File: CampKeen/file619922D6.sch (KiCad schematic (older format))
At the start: 40 parts, among them Q20 2N7000, Q21 2N7000, Q22 2N7000, Q23 2N7000, Q24 2N7000, Q25 2N7000, Q26 2N7000, Q27 2N7000, Q28 2N7000, Q29 2N7000

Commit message: some annotation.
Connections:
- net +5V renamed +5VL
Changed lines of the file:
@@
 Wire Wire Line
 	2450 1600 2450 1550
-$Comp
-L power:+5V #PWR?
-U 1 1 61994D03
-P 2450 950
-AR Path="/62665296/61994D03" Ref="#PWR?"  Part="1"
-AR Path="/6479D118/61994D03" Ref="#PWR?"  Part="1"
-AR Path="/627AE565/61994D03" Ref="#PWR?"  Part="1"
-AR Path="/619922D7/61994D03" Ref="#PWR0105"  Part="1"
-F 0 "#PWR0105" H 2450 800 50  0001 C CNN
-F 1 "+5V" H 2465 1123 50  0000 C CNN
-F 2 "" H 2450 950 50  0001 C CNN
-F 3 "" H 2450 950 50  0001 C CNN
-	1    2450 950
-	1    0    0    -1
-$EndComp
 Wire Wire Line
 	2450 1100 2450 950
@@
 Wire Wire Line
 	2450 3300 2450 3250
-$Comp
-L power:+5V #PWR?
-U 1 1 619C5CF6
-P 2450 2650
-AR Path="/62665296/619C5CF6" Ref="#PWR?"  Part="1"
-AR Path="/6479D118/619C5CF6" Ref="#PWR?"  Part="1"
-AR Path="/627AE565/619C5CF6" Ref="#PWR?"  Part="1"
-AR Path="/619922D7/619C5CF6" Ref="#PWR0107"  Part="1"
-F 0 "#PWR0107" H 2450 2500 50  0001 C CNN
-F 1 "+5V" H 2465 2823 50  0000 C CNN
-F 2 "" H 2450 2650 50  0001 C CNN
-F 3 "" H 2450 2650 50  0001 C CNN
-	1    2450 2650
-	1    0    0    -1
-$EndComp
 Wire Wire Line
 	2450 2800 2450 2650
@@
 Wire Wire Line
 	2450 4900 2450 4850
-$Comp
-L power:+5V #PWR?
-U 1 1 619F4CB4
-P 2450 4250
-AR Path="/62665296/619F4CB4" Ref="#PWR?"  Part="1"
-AR Path="/6479D118/619F4CB4" Ref="#PWR?"  Part="1"
-AR Path="/627AE565/619F4CB4" Ref="#PWR?"  Part="1"
-AR Path="/619922D7/619F4CB4" Ref="#PWR0109"  Part="1"
-F 0 "#PWR0109" H 2450 4100 50  0001 C CNN
-F 1 "+5V" H 2465 4423 50  0000 C CNN
-F 2 "" H 2450 4250 50  0001 C CNN
-F 3 "" H 2450 4250 50  0001 C CNN
-	1    2450 4250
-	1    0    0    -1
-$EndComp
 Wire Wire Line
 	2450 4400 2450 4250
@@
 Wire Wire Line
 	2450 6600 2450 6550
-$Comp
-L power:+5V #PWR?
-U 1 1 619FB7BE
-P 2450 5950
-AR Path="/62665296/619FB7BE" Ref="#PWR?"  Part="1"
-AR Path="/6479D118/619FB7BE" Ref="#PWR?"  Part="1"
-AR Path="/627AE565/619FB7BE" Ref="#PWR?"  Part="1"
-AR Path="/619922D7/619FB7BE" Ref="#PWR0111"  Part="1"
-F 0 "#PWR0111" H 2450 5800 50  0001 C CNN
-F 1 "+5V" H 2465 6123 50  0000 C CNN
-F 2 "" H 2450 5950 50  0001 C CNN
-F 3 "" H 2450 5950 50  0001 C CNN
-	1    2450 5950
-	1    0    0    -1
-$EndComp
 Wire Wire Line
 	2450 6100 2450 5950
@@
 Wire Wire Line
 	5750 1600 5750 1550
-$Comp
-L power:+5V #PWR?
-U 1 1 61AA89BA
-P 5750 950
-AR Path="/62665296/61AA89BA" Ref="#PWR?"  Part="1"
-AR Path="/6479D118/61AA89BA" Ref="#PWR?"  Part="1"
-AR Path="/627AE565/61AA89BA" Ref="#PWR?"  Part="1"
-AR Path="/619922D7/61AA89BA" Ref="#PWR0113"  Part="1"
-F 0 "#PWR0113" H 5750 800 50  0001 C CNN
-F 1 "+5V" H 5765 1123 50  0000 C CNN
-F 2 "" H 5750 950 50  0001 C CNN
-F 3 "" H 5750 950 50  0001 C CNN
-	1    5750 950
-	1    0    0    -1
-$EndComp
 Wire Wire Line
 	5750 1100 5750 950
@@
 Wire Wire Line
 	8150 1600 8150 1550
-$Comp
-L power:+5V #PWR?
-U 1 1 61AC655C
-P 8150 950
-AR Path="/62665296/61AC655C" Ref="#PWR?"  Part="1"
-AR Path="/6479D118/61AC655C" Ref="#PWR?"  Part="1"
-AR Path="/627AE565/61AC655C" Ref="#PWR?"  Part="1"
-AR Path="/619922D7/61AC655C" Ref="#PWR0121"  Part="1"
-F 0 "#PWR0121" H 8150 800 50  0001 C CNN
-F 1 "+5V" H 8165 1123 50  0000 C CNN
-F 2 "" H 8150 950 50  0001 C CNN
-F 3 "" H 8150 950 50  0001 C CNN
-	1    8150 950
-	1    0    0    -1
-$EndComp
 Wire Wire Line
 	8150 1100 8150 950
@@
 Wire Wire Line
 	5750 3350 5750 3300
-$Comp
-L power:+5V #PWR?
-U 1 1 61ACB046
-P 5750 2700
-AR Path="/62665296/61ACB046" Ref="#PWR?"  Part="1"
-AR Path="/6479D118/61ACB046" Ref="#PWR?"  Part="1"
-AR Path="/627AE565/61ACB046" Ref="#PWR?"  Part="1"
-AR Path="/619922D7/61ACB046" Ref="#PWR0115"  Part="1"
-F 0 "#PWR0115" H 5750 2550 50  0001 C CNN
-F 1 "+5V" H 5765 2873 50  0000 C CNN
-F 2 "" H 5750 2700 50  0001 C CNN
-F 3 "" H 5750 2700 50  0001 C CNN
-	1    5750 2700
-	1    0    0    -1
-$EndComp
 Wire Wire Line
 	5750 2850 5750 2700
@@
 Wire Wire Line
 	8150 3350 8150 3300
-$Comp
-L power:+5V #PWR?
-U 1 1 61ACFF01
-P 8150 2700
-AR Path="/62665296/61ACFF01" Ref="#PWR?"  Part="1"
-AR Path="/6479D118/61ACFF01" Ref="#PWR?"  Part="1"
-AR Path="/627AE565/61ACFF01" Ref="#PWR?"  Part="1"
-AR Path="/619922D7/61ACFF01" Ref="#PWR0123"  Part="1"
-F 0 "#PWR0123" H 8150 2550 50  0001 C CNN
-F 1 "+5V" H 8165 2873 50  0000 C CNN
-F 2 "" H 8150 2700 50  0001 C CNN
-F 3 "" H 8150 2700 50  0001 C CNN
-	1    8150 2700
-	1    0    0    -1
-$EndComp
 Wire Wire Line
 	8150 2850 8150 2700
@@
 Wire Wire Line
 	5750 5100 5750 5050
-$Comp
-L power:+5V #PWR?
-U 1 1 61AD6017
-P 5750 4450
-AR Path="/62665296/61AD6017" Ref="#PWR?"  Part="1"
-AR Path="/6479D118/61AD6017" Ref="#PWR?"  Part="1"
-AR Path="/627AE565/61AD6017" Ref="#PWR?"  Part="1"
-AR Path="/619922D7/61AD6017" Ref="#PWR0117"  Part="1"
-F 0 "#PWR0117" H 5750 4300 50  0001 C CNN
-F 1 "+5V" H 5765 4623 50  0000 C CNN
-F 2 "" H 5750 4450 50  0001 C CNN
-F 3 "" H 5750 4450 50  0001 C CNN
-	1    5750 4450
-	1    0    0    -1
-$EndComp
 Wire Wire Line
 	5750 4600 5750 4450
@@
 Wire Wire Line
 	8100 5100 8100 5050
-$Comp
-L power:+5V #PWR?
-U 1 1 61ADB4DA
-P 8100 4450
-AR Path="/62665296/61ADB4DA" Ref="#PWR?"  Part="1"
-AR Path="/6479D118/61ADB4DA" Ref="#PWR?"  Part="1"
-AR Path="/627AE565/61ADB4DA" Ref="#PWR?"  Part="1"
-AR Path="/619922D7/61ADB4DA" Ref="#PWR0119"  Part="1"
-F 0 "#PWR0119" H 8100 4300 50  0001 C CNN
-F 1 "+5V" H 8115 4623 50  0000 C CNN
-F 2 "" H 8100 4450 50  0001 C CNN
-F 3 "" H 8100 4450 50  0001 C CNN
-	1    8100 4450
-	1    0    0    -1
-$EndComp
 Wire Wire Line
 	8100 4600 8100 4450
@@
 Wire Wire Line
 	7150 5100 7150 4800
+$Comp
+L power:+5VL #PWR0107
+U 1 1 61BBDD38
+P 2450 950
+F 0 "#PWR0107" H 2450 800 50  0001 C CNN
+F 1 "+5VL" H 2465 1123 50  0000 C CNN
+F 2 "" H 2450 950 50  0001 C CNN
+F 3 "" H 2450 950 50  0001 C CNN
+	1    2450 950
+	1    0    0    -1
+$EndComp
+$Comp
+L power:+5VL #PWR0115
+U 1 1 61BC5B51
+P 5750 950
+F 0 "#PWR0115" H 5750 800 50  0001 C CNN
+F 1 "+5VL" H 5765 1123 50  0000 C CNN
+F 2 "" H 5750 950 50  0001 C CNN
+F 3 "" H 5750 950 50  0001 C CNN
+	1    5750 950
+	1    0    0    -1
+$EndComp
+$Comp
+L power:+5VL #PWR0123
+U 1 1 61BCD965
+P 8150 950
+F 0 "#PWR0123" H 8150 800 50  0001 C CNN
+F 1 "+5VL" H 8165 1123 50  0000 C CNN
+F 2 "" H 8150 950 50  0001 C CNN
+F 3 "" H 8150 950 50  0001 C CNN
+	1    8150 950
+	1    0    0    -1
+$EndComp
+$Comp
+L power:+5VL #PWR0153
+U 1 1 61BD57E2
+P 8150 2700
+F 0 "#PWR0153" H 8150 2550 50  0001 C CNN
+F 1 "+5VL" H 8165 2873 50  0000 C CNN
+F 2 "" H 8150 2700 50  0001 C CNN
+F 3 "" H 8150 2700 50  0001 C CNN
+	1    8150 2700
+	1    0    0    -1
+$EndComp
+$Comp
+L power:+5VL #PWR0117
+U 1 1 61BDD617
+P 5750 2700
+F 0 "#PWR0117" H 5750 2550 50  0001 C CNN
+F 1 "+5VL" H 5765 2873 50  0000 C CNN
+F 2 "" H 5750 2700 50  0001 C CNN
+F 3 "" H 5750 2700 50  0001 C CNN
+	1    5750 2700
+	1    0    0    -1
+$EndComp
+$Comp
+L power:+5VL #PWR0109
+U 1 1 61BE57AF
+P 2450 2650
+F 0 "#PWR0109" H 2450 2500 50  0001 C CNN
+F 1 "+5VL" H 2465 2823 50  0000 C CNN
+F 2 "" H 2450 2650 50  0001 C CNN
+F 3 "" H 2450 2650 50  0001 C CNN
+	1    2450 2650
+	1    0    0    -1
+$EndComp
+$Comp
+L power:+5VL #PWR0111
+U 1 1 61BED6DC
+P 2450 4250
+F 0 "#PWR0111" H 2450 4100 50  0001 C CNN
+F 1 "+5VL" H 2465 4423 50  0000 C CNN
+F 2 "" H 2450 4250 50  0001 C CNN
+F 3 "" H 2450 4250 50  0001 C CNN
+	1    2450 4250
+	1    0    0    -1
+$EndComp
+$Comp
+L power:+5VL #PWR0121
+U 1 1 61BF9767
+P 8100 4450
+F 0 "#PWR0121" H 8100 4300 50  0001 C CNN
+F 1 "+5VL" H 8115 4623 50  0000 C CNN
+F 2 "" H 8100 4450 50  0001 C CNN
+F 3 "" H 8100 4450 50  0001 C CNN
+	1    8100 4450
+	1    0    0    -1
+$EndComp
+$Comp
+L power:+5VL #PWR0119
+U 1 1 61C01846
+P 5750 4450
+F 0 "#PWR0119" H 5750 4300 50  0001 C CNN
+F 1 "+5VL" H 5765 4623 50  0000 C CNN
+F 2 "" H 5750 4450 50  0001 C CNN
+F 3 "" H 5750 4450 50  0001 C CNN
+	1    5750 4450
+	1    0    0    -1
+$EndComp
+$Comp
+L power:+5VL #PWR0113
+U 1 1 61C09647
+P 2450 5950
+F 0 "#PWR0113" H 2450 5800 50  0001 C CNN
+F 1 "+5VL" H 2465 6123 50  0000 C CNN
+F 2 "" H 2450 5950 50  0001 C CNN
+F 3 "" H 2450 5950 50  0001 C CNN
+	1    2450 5950
+	1    0    0    -1
+$EndComp
 $EndSCHEMATC

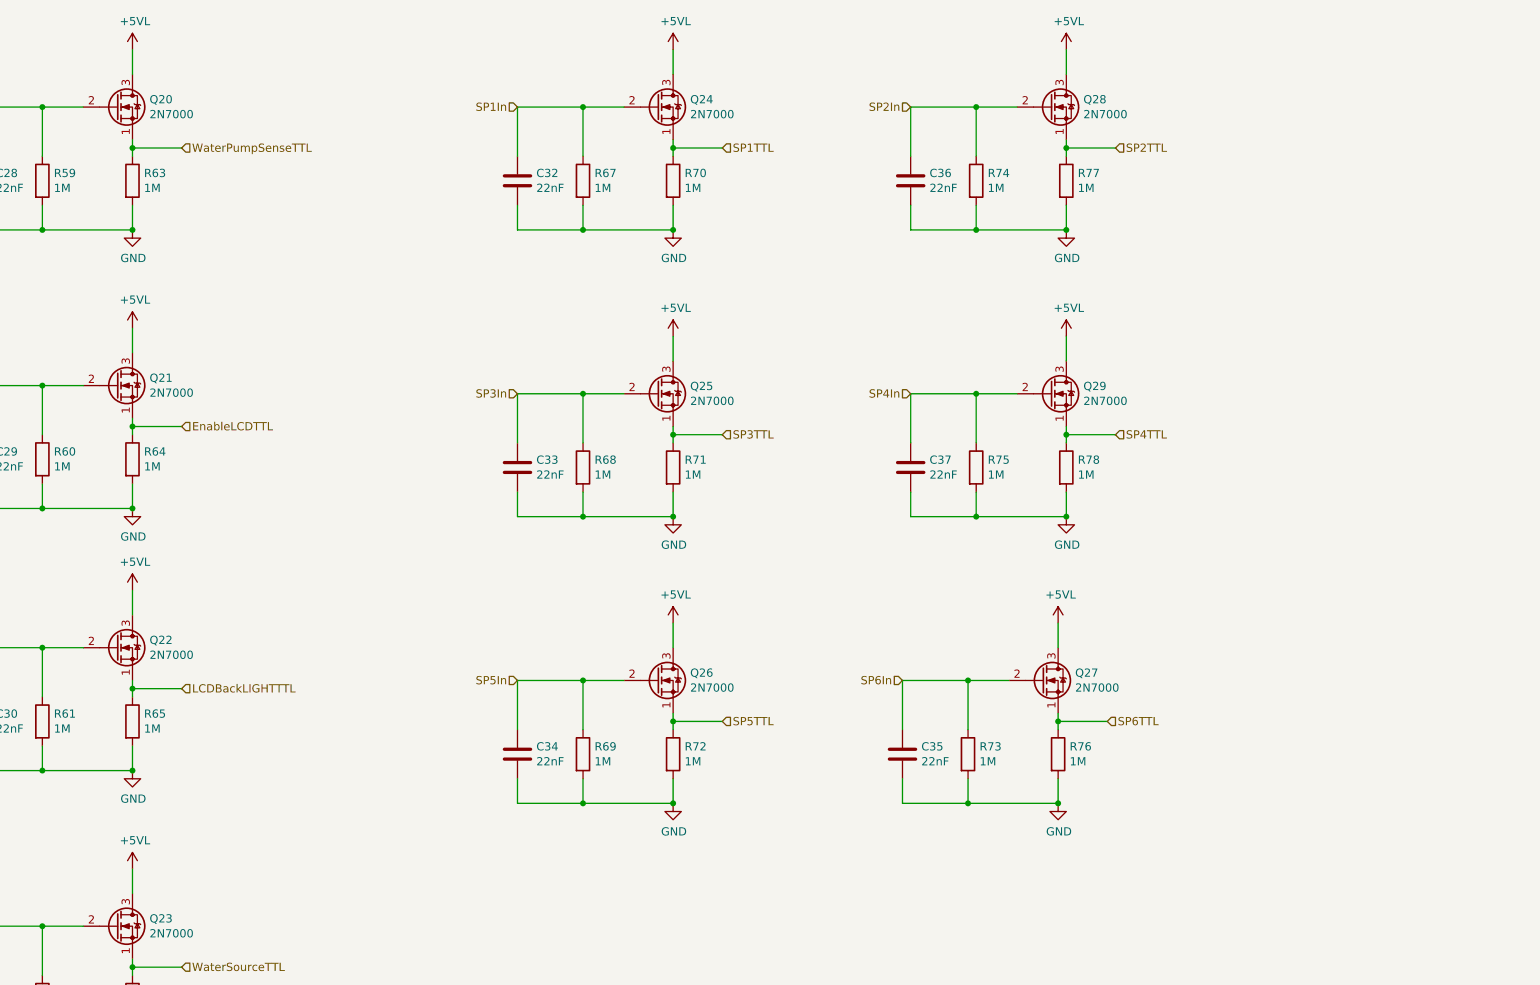
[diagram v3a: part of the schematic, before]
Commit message: wip for working on the input circuits on the board. they are getting upgraded with opto-isolation as i've found that you can burn out the processor board if there is a voltage applied to an input when the system is on and then turned off. for the code fixing some of the LCD display code.
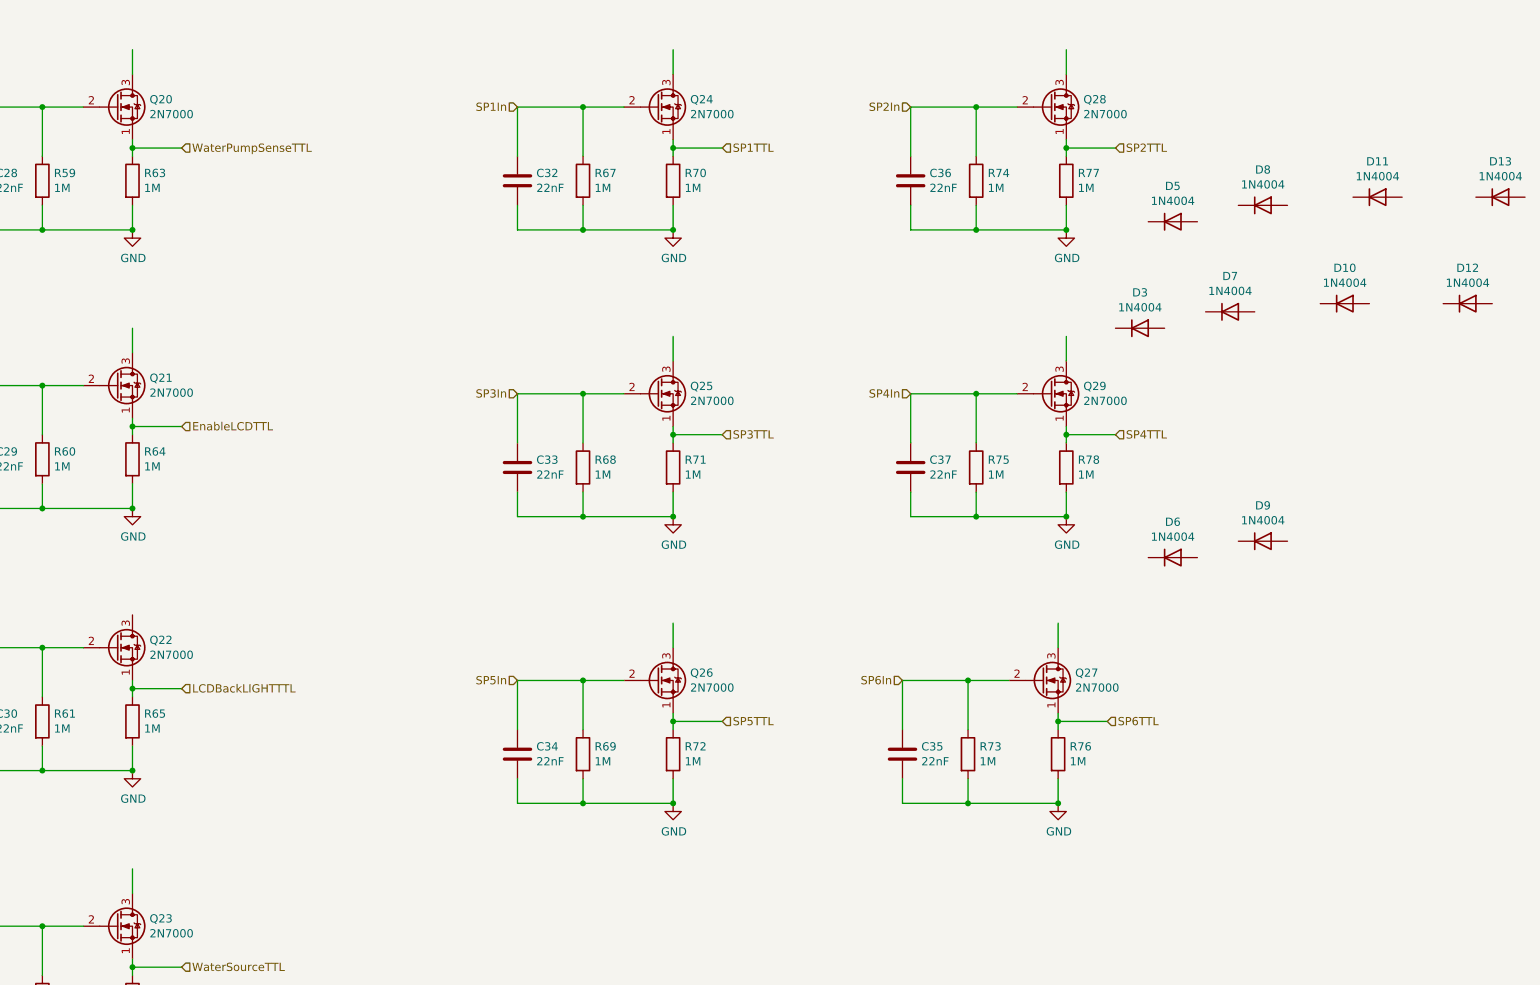
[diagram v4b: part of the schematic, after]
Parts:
- added D10, D11, D12, D13, D3, D5, D6, D7, D8, D9: 1N4004, Diode_THT:D_DO-41_SOD81_P10.16mm_Horizontal, symbol Diode:1N4004
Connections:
- net labels removed: +5VL
- wire segments 130 -> 129
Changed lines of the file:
@@
 	2450 4900 2450 4850
-Wire Wire Line
-	2450 4400 2450 4250
 Wire Wire Line
 	2450 4850 2750 4850
@@
 	7150 5100 7150 4800
 $Comp
-L power:+5VL #PWR0107
-U 1 1 61BBDD38
-P 2450 950
-F 0 "#PWR0107" H 2450 800 50  0001 C CNN
-F 1 "+5VL" H 2465 1123 50  0000 C CNN
-F 2 "" H 2450 950 50  0001 C CNN
-F 3 "" H 2450 950 50  0001 C CNN
-	1    2450 950
-	1    0    0    -1
-$EndComp
-$Comp
-L power:+5VL #PWR0115
-U 1 1 61BC5B51
-P 5750 950
-F 0 "#PWR0115" H 5750 800 50  0001 C CNN
-F 1 "+5VL" H 5765 1123 50  0000 C CNN
-F 2 "" H 5750 950 50  0001 C CNN
-F 3 "" H 5750 950 50  0001 C CNN
-	1    5750 950
-	1    0    0    -1
-$EndComp
-$Comp
-L power:+5VL #PWR0123
-U 1 1 61BCD965
-P 8150 950
-F 0 "#PWR0123" H 8150 800 50  0001 C CNN
-F 1 "+5VL" H 8165 1123 50  0000 C CNN
-F 2 "" H 8150 950 50  0001 C CNN
-F 3 "" H 8150 950 50  0001 C CNN
-	1    8150 950
-	1    0    0    -1
-$EndComp
-$Comp
-L power:+5VL #PWR0153
-U 1 1 61BD57E2
-P 8150 2700
-F 0 "#PWR0153" H 8150 2550 50  0001 C CNN
-F 1 "+5VL" H 8165 2873 50  0000 C CNN
-F 2 "" H 8150 2700 50  0001 C CNN
-F 3 "" H 8150 2700 50  0001 C CNN
-	1    8150 2700
-	1    0    0    -1
-$EndComp
-$Comp
-L power:+5VL #PWR0117
-U 1 1 61BDD617
-P 5750 2700
-F 0 "#PWR0117" H 5750 2550 50  0001 C CNN
-F 1 "+5VL" H 5765 2873 50  0000 C CNN
-F 2 "" H 5750 2700 50  0001 C CNN
-F 3 "" H 5750 2700 50  0001 C CNN
-	1    5750 2700
-	1    0    0    -1
-$EndComp
-$Comp
-L power:+5VL #PWR0109
-U 1 1 61BE57AF
-P 2450 2650
-F 0 "#PWR0109" H 2450 2500 50  0001 C CNN
-F 1 "+5VL" H 2465 2823 50  0000 C CNN
-F 2 "" H 2450 2650 50  0001 C CNN
-F 3 "" H 2450 2650 50  0001 C CNN
-	1    2450 2650
-	1    0    0    -1
-$EndComp
-$Comp
-L power:+5VL #PWR0111
-U 1 1 61BED6DC
-P 2450 4250
-F 0 "#PWR0111" H 2450 4100 50  0001 C CNN
-F 1 "+5VL" H 2465 4423 50  0000 C CNN
-F 2 "" H 2450 4250 50  0001 C CNN
-F 3 "" H 2450 4250 50  0001 C CNN
-	1    2450 4250
-	1    0    0    -1
-$EndComp
-$Comp
-L power:+5VL #PWR0121
-U 1 1 61BF9767
-P 8100 4450
-F 0 "#PWR0121" H 8100 4300 50  0001 C CNN
-F 1 "+5VL" H 8115 4623 50  0000 C CNN
-F 2 "" H 8100 4450 50  0001 C CNN
-F 3 "" H 8100 4450 50  0001 C CNN
-	1    8100 4450
-	1    0    0    -1
-$EndComp
-$Comp
-L power:+5VL #PWR0119
-U 1 1 61C01846
-P 5750 4450
-F 0 "#PWR0119" H 5750 4300 50  0001 C CNN
-F 1 "+5VL" H 5765 4623 50  0000 C CNN
-F 2 "" H 5750 4450 50  0001 C CNN
-F 3 "" H 5750 4450 50  0001 C CNN
-	1    5750 4450
-	1    0    0    -1
-$EndComp
-$Comp
-L power:+5VL #PWR0113
-U 1 1 61C09647
-P 2450 5950
-F 0 "#PWR0113" H 2450 5800 50  0001 C CNN
-F 1 "+5VL" H 2465 6123 50  0000 C CNN
-F 2 "" H 2450 5950 50  0001 C CNN
-F 3 "" H 2450 5950 50  0001 C CNN
-	1    2450 5950
-	1    0    0    -1
-$EndComp
+L Diode:1N4004 D?
+U 1 1 61CCCAE6
+P 8600 2650
+AR Path="/6479D118/61CCCAE6" Ref="D?"  Part="1"
+AR Path="/619922D7/61CCCAE6" Ref="D3"  Part="1"
+F 0 "D3" H 8600 2867 50  0000 C CNN
+F 1 "1N4004" H 8600 2776 50  0000 C CNN
+F 2 "Diode_THT:D_DO-41_SOD81_P10.16mm_Horizontal" H 8600 2475 50  0001 C CNN
+F 3 "http://www.vishay.com/docs/88503/1n4001.pdf" H 8600 2650 50  0001 C CNN
+	1    8600 2650
+	1    0    0    -1
+$EndComp
+$Comp
+L Diode:1N4004 D?
+U 1 1 61CCCAEC
+P 9150 2550
+AR Path="/6479D118/61CCCAEC" Ref="D?"  Part="1"
+AR Path="/619922D7/61CCCAEC" Ref="D7"  Part="1"
+F 0 "D7" H 9150 2767 50  0000 C CNN
+F 1 "1N4004" H 9150 2676 50  0000 C CNN
+F 2 "Diode_THT:D_DO-41_SOD81_P10.16mm_Horizontal" H 9150 2375 50  0001 C CNN
+F 3 "http://www.vishay.com/docs/88503/1n4001.pdf" H 9150 2550 50  0001 C CNN
+	1    9150 2550
+	1    0    0    -1
+$EndComp
+$Comp
+L Diode:1N4004 D?
+U 1 1 61CCCAF2
+P 9850 2500
+AR Path="/6479D118/61CCCAF2" Ref="D?"  Part="1"
+AR Path="/619922D7/61CCCAF2" Ref="D10"  Part="1"
+F 0 "D10" H 9850 2717 50  0000 C CNN
+F 1 "1N4004" H 9850 2626 50  0000 C CNN
+F 2 "Diode_THT:D_DO-41_SOD81_P10.16mm_Horizontal" H 9850 2325 50  0001 C CNN
+F 3 "http://www.vishay.com/docs/88503/1n4001.pdf" H 9850 2500 50  0001 C CNN
+	1    9850 2500
+	1    0    0    -1
+$EndComp
+$Comp
+L Diode:1N4004 D?
+U 1 1 61CCCAF8
+P 10600 2500
+AR Path="/6479D118/61CCCAF8" Ref="D?"  Part="1"
+AR Path="/619922D7/61CCCAF8" Ref="D12"  Part="1"
+F 0 "D12" H 10600 2717 50  0000 C CNN
+F 1 "1N4004" H 10600 2626 50  0000 C CNN
+F 2 "Diode_THT:D_DO-41_SOD81_P10.16mm_Horizontal" H 10600 2325 50  0001 C CNN
+F 3 "http://www.vishay.com/docs/88503/1n4001.pdf" H 10600 2500 50  0001 C CNN
+	1    10600 2500
+	1    0    0    -1
+$EndComp
+$Comp
+L Diode:1N4004 D?
+U 1 1 61CD23F7
+P 8800 2000
+AR Path="/6479D118/61CD23F7" Ref="D?"  Part="1"
+AR Path="/619922D7/61CD23F7" Ref="D5"  Part="1"
+F 0 "D5" H 8800 2217 50  0000 C CNN
+F 1 "1N4004" H 8800 2126 50  0000 C CNN
+F 2 "Diode_THT:D_DO-41_SOD81_P10.16mm_Horizontal" H 8800 1825 50  0001 C CNN
+F 3 "http://www.vishay.com/docs/88503/1n4001.pdf" H 8800 2000 50  0001 C CNN
+	1    8800 2000
+	1    0    0    -1
+$EndComp
+$Comp
+L Diode:1N4004 D?
+U 1 1 61CD23FD
+P 9350 1900
+AR Path="/6479D118/61CD23FD" Ref="D?"  Part="1"
+AR Path="/619922D7/61CD23FD" Ref="D8"  Part="1"
+F 0 "D8" H 9350 2117 50  0000 C CNN
+F 1 "1N4004" H 9350 2026 50  0000 C CNN
+F 2 "Diode_THT:D_DO-41_SOD81_P10.16mm_Horizontal" H 9350 1725 50  0001 C CNN
+F 3 "http://www.vishay.com/docs/88503/1n4001.pdf" H 9350 1900 50  0001 C CNN
+	1    9350 1900
+	1    0    0    -1
+$EndComp
+$Comp
+L Diode:1N4004 D?
+U 1 1 61CD2403
+P 10050 1850
+AR Path="/6479D118/61CD2403" Ref="D?"  Part="1"
+AR Path="/619922D7/61CD2403" Ref="D11"  Part="1"
+F 0 "D11" H 10050 2067 50  0000 C CNN
+F 1 "1N4004" H 10050 1976 50  0000 C CNN
+F 2 "Diode_THT:D_DO-41_SOD81_P10.16mm_Horizontal" H 10050 1675 50  0001 C CNN
+F 3 "http://www.vishay.com/docs/88503/1n4001.pdf" H 10050 1850 50  0001 C CNN
+	1    10050 1850
+	1    0    0    -1
+$EndComp
+$Comp
+L Diode:1N4004 D?
+U 1 1 61CD2409
+P 10800 1850
+AR Path="/6479D118/61CD2409" Ref="D?"  Part="1"
+AR Path="/619922D7/61CD2409" Ref="D13"  Part="1"
+F 0 "D13" H 10800 2067 50  0000 C CNN
+F 1 "1N4004" H 10800 1976 50  0000 C CNN
+F 2 "Diode_THT:D_DO-41_SOD81_P10.16mm_Horizontal" H 10800 1675 50  0001 C CNN
+F 3 "http://www.vishay.com/docs/88503/1n4001.pdf" H 10800 1850 50  0001 C CNN
+	1    10800 1850
+	1    0    0    -1
+$EndComp
+$Comp
+L Diode:1N4004 D?
+U 1 1 61CD7318
+P 8800 4050
+AR Path="/6479D118/61CD7318" Ref="D?"  Part="1"
+AR Path="/619922D7/61CD7318" Ref="D6"  Part="1"
+F 0 "D6" H 8800 4267 50  0000 C CNN
+F 1 "1N4004" H 8800 4176 50  0000 C CNN
+F 2 "Diode_THT:D_DO-41_SOD81_P10.16mm_Horizontal" H 8800 3875 50  0001 C CNN
+F 3 "http://www.vishay.com/docs/88503/1n4001.pdf" H 8800 4050 50  0001 C CNN
+	1    8800 4050
+	1    0    0    -1
+$EndComp
+$Comp
+L Diode:1N4004 D?
+U 1 1 61CD731E
+P 9350 3950
+AR Path="/6479D118/61CD731E" Ref="D?"  Part="1"
+AR Path="/619922D7/61CD731E" Ref="D9"  Part="1"
+F 0 "D9" H 9350 4167 50  0000 C CNN
+F 1 "1N4004" H 9350 4076 50  0000 C CNN
+F 2 "Diode_THT:D_DO-41_SOD81_P10.16mm_Horizontal" H 9350 3775 50  0001 C CNN
+F 3 "http://www.vishay.com/docs/88503/1n4001.pdf" H 9350 3950 50  0001 C CNN
+	1    9350 3950
+	1    0    0    -1
+$EndComp
